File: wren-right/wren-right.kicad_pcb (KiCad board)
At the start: 2 copper layers, 93 parts, among them J1 TRRS_Jack, SW0 Reset, U1 ProMicro

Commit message: Tracks Finished
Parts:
- MX41: footprint MX_Only:MX-2U -> MX_Only:MX-2U-FLIPPED-ReversedStabilizers
- SW0: footprint random-keyboard-parts:SKQG-1155865 -> Button_Switch_THT:SW_PUSH_6mm; moved to F.Cu
- U1: moved to B.Cu
- moved R1 36.4 mm to (241.0, 33.8)
- moved R2 24.5 mm to (241.2, 46.0)
- moved SW0 3.97 mm to (238.1, 60.3)
- moved D13 2.38 mm to (190.5, 50.0)
- moved D3 2.38 mm to (190.5, 31.0)
- moved D23 2.38 mm to (190.5, 69.1)
- moved D33 2.38 mm to (190.5, 88.1)
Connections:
- U1 pad 1: COL8 -> ROW0
- U1 pad 10: ROW3 -> COL9
- U1 pad 11: ROW4 -> Net-(U1-Pad11)
- U1 pad 12: Net-(U1-Pad12) -> ROW4
- U1 pad 13: COL7 -> COL0
- U1 pad 14: COL6 -> COL1
- U1 pad 15: COL5 -> COL2
- U1 pad 16: COL4 -> COL3
- U1 pad 17: COL3 -> COL4
- U1 pad 18: COL2 -> COL5
- U1 pad 19: COL1 -> COL6
- U1 pad 2: COL9 -> ROW1
- U1 pad 20: COL0 -> COL7
- U1 pad 7: ROW0 -> ROW2
- U1 pad 8: ROW1 -> ROW3
- U1 pad 9: ROW2 -> COL8
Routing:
- net COL9: track 0.00 -> 265.9 mm, vias 0 -> 1
- net COL8: track 0.00 -> 247.9 mm, vias 0 -> 1
- net ROW3: track 0.00 -> 244.9 mm, vias 0 -> 1
- net ROW2: track 0.00 -> 227.9 mm, vias 0 -> 1
- net ROW1: track 0.00 -> 222.3 mm, vias 0 -> 1
- net ROW0: track 0.00 -> 211.7 mm, vias 0 -> 1
- net COL7: track 0.00 -> 210.2 mm, vias 0 -> 2
- net COL6: track 0.00 -> 192.4 mm, vias 0 -> 1
- net COL5: track 0.00 -> 170.9 mm, vias 0 -> 1
- net COL3: track 0.00 -> 164.6 mm
- net COL4: track 0.00 -> 152.9 mm, vias 0 -> 3
- net COL2: track 0.00 -> 149.9 mm, vias 0 -> 3
- net ROW4: track 0.00 -> 131.7 mm, vias 0 -> 1
- net COL1: track 0.00 -> 125.5 mm, vias 0 -> 1
- net COL0: track 0.00 -> 109.9 mm, vias 0 -> 1
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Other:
- board outline added: 230.3 x 117 mm

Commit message: Left Side Finished
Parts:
- removed D10, D17, D18, D19, D20, D27, D28, D29, D30, D37, D38, D39, D40, D7, D8, D9: D_Small, Diode_SMD:D_SOD-123
- removed MX10, MX17, MX18, MX19, MX20, MX27, MX28, MX29, MX30, MX37, MX38, MX39, MX40, MX7, MX8, MX9: MX-NoLED, MX_Only:MX-1U
- D1, D11, D12, D13, D14, D15, D16, D2, D21, D22, D23, D24, D25, D26, D3, D31, D32, D33, D34, D35, D36, D4, D41, D42, D43, D44, D5, D6, R1, R2, U1: moved to F.Cu
- J1, MX1, MX11, MX12, MX13, MX14, MX15, MX16, MX2, MX21, MX22, MX23, MX24, MX25, MX26, MX3, MX31, MX32, MX33, MX34, MX35, MX36, MX4, MX41, MX42, MX43, MX44, MX5, MX6, SW0: moved to B.Cu
- moved J1 198.3 mm to (58.4, 118.2), turned to 210 degrees
- moved D41 177.8 mm to (68.7, 130.1), turned to 30 degrees
- moved MX41 169.9 mm to (72.6, 137.3), turned to 120 degrees
- moved U1 169.9 mm to (72.6, 62.7)
- moved R2 169.7 mm to (72.8, 66.6), turned to 0 degrees
- moved R1 169.4 mm to (72.9, 54.4), turned to 0 degrees
- moved SW0 163.6 mm to (75.8, 80.9), turned to 180 degrees
- moved D1 144.7 mm to (85.3, 56.3)
- moved D11 144.7 mm to (85.3, 75.4)
- moved D21 144.7 mm to (85.3, 94.4)
- moved D31 144.7 mm to (85.3, 113.5)
- moved MX1 129.0 mm to (93.3, 56.3), turned to 180 degrees
- moved MX11 129.0 mm to (93.3, 75.4), turned to 180 degrees
- moved MX21 129.0 mm to (93.3, 94.4), turned to 180 degrees
- moved MX31 129.0 mm to (93.3, 113.5), turned to 180 degrees
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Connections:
- U1 pad 10: COL9 -> Net-(U1-Pad10)
- U1 pad 12: ROW4 -> Net-(U1-Pad12)
- U1 pad 19: COL6 -> Net-(U1-Pad19)
- U1 pad 20: COL7 -> Net-(U1-Pad20)
- U1 pad 9: COL8 -> Net-(U1-Pad9)
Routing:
- net COL9: track 265.9 -> 0.00 mm, vias 1 -> 0
- net COL8: track 247.9 -> 0.00 mm, vias 1 -> 0
- net ROW3: track 244.9 -> 0.00 mm, vias 1 -> 0
- net ROW2: track 227.9 -> 0.00 mm, vias 1 -> 0
- net ROW1: track 222.3 -> 0.00 mm, vias 1 -> 0
- net ROW0: track 211.7 -> 0.00 mm, vias 1 -> 0
- net COL7: track 210.2 -> 0.00 mm, vias 2 -> 0
- net COL6: track 192.4 -> 0.00 mm, vias 1 -> 0
- net COL5: track 170.9 -> 0.00 mm, vias 1 -> 0
- net COL3: track 164.6 -> 0.00 mm
- net COL4: track 152.9 -> 0.00 mm, vias 3 -> 0
- net COL2: track 149.9 -> 0.00 mm, vias 3 -> 0
- net ROW4: track 131.7 -> 0.00 mm, vias 1 -> 0
- net COL1: track 125.5 -> 0.00 mm, vias 1 -> 0
- net COL0: track 109.9 -> 0.00 mm, vias 1 -> 0
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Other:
- board size 230.3 x 117 mm -> 132.7 x 117 mm

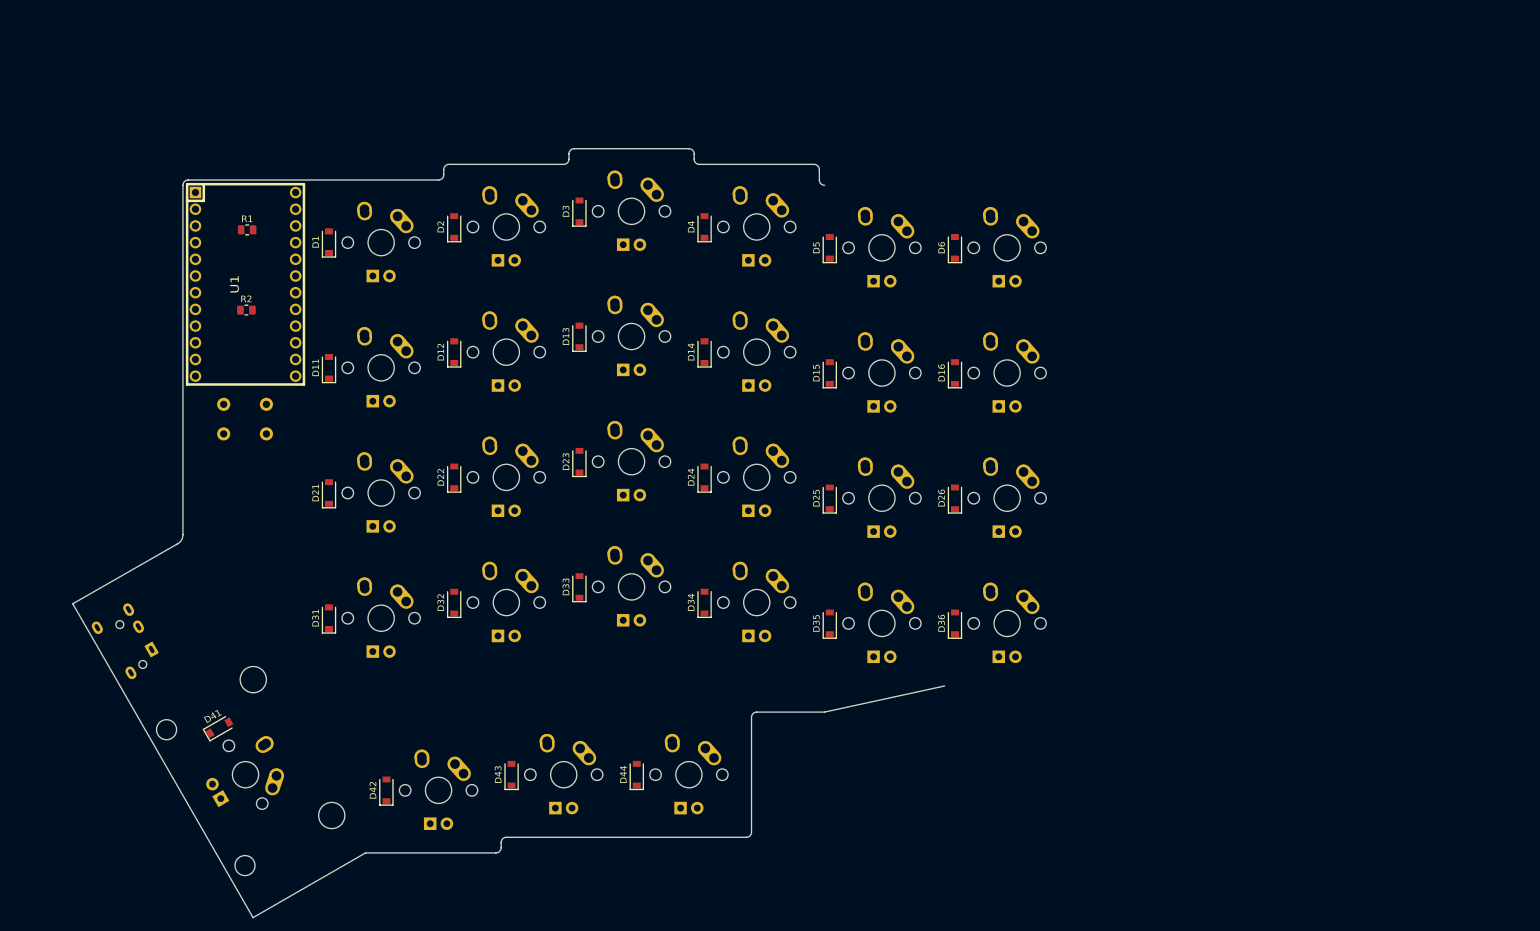
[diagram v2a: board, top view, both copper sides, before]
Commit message: Added Mirrored Right PCB
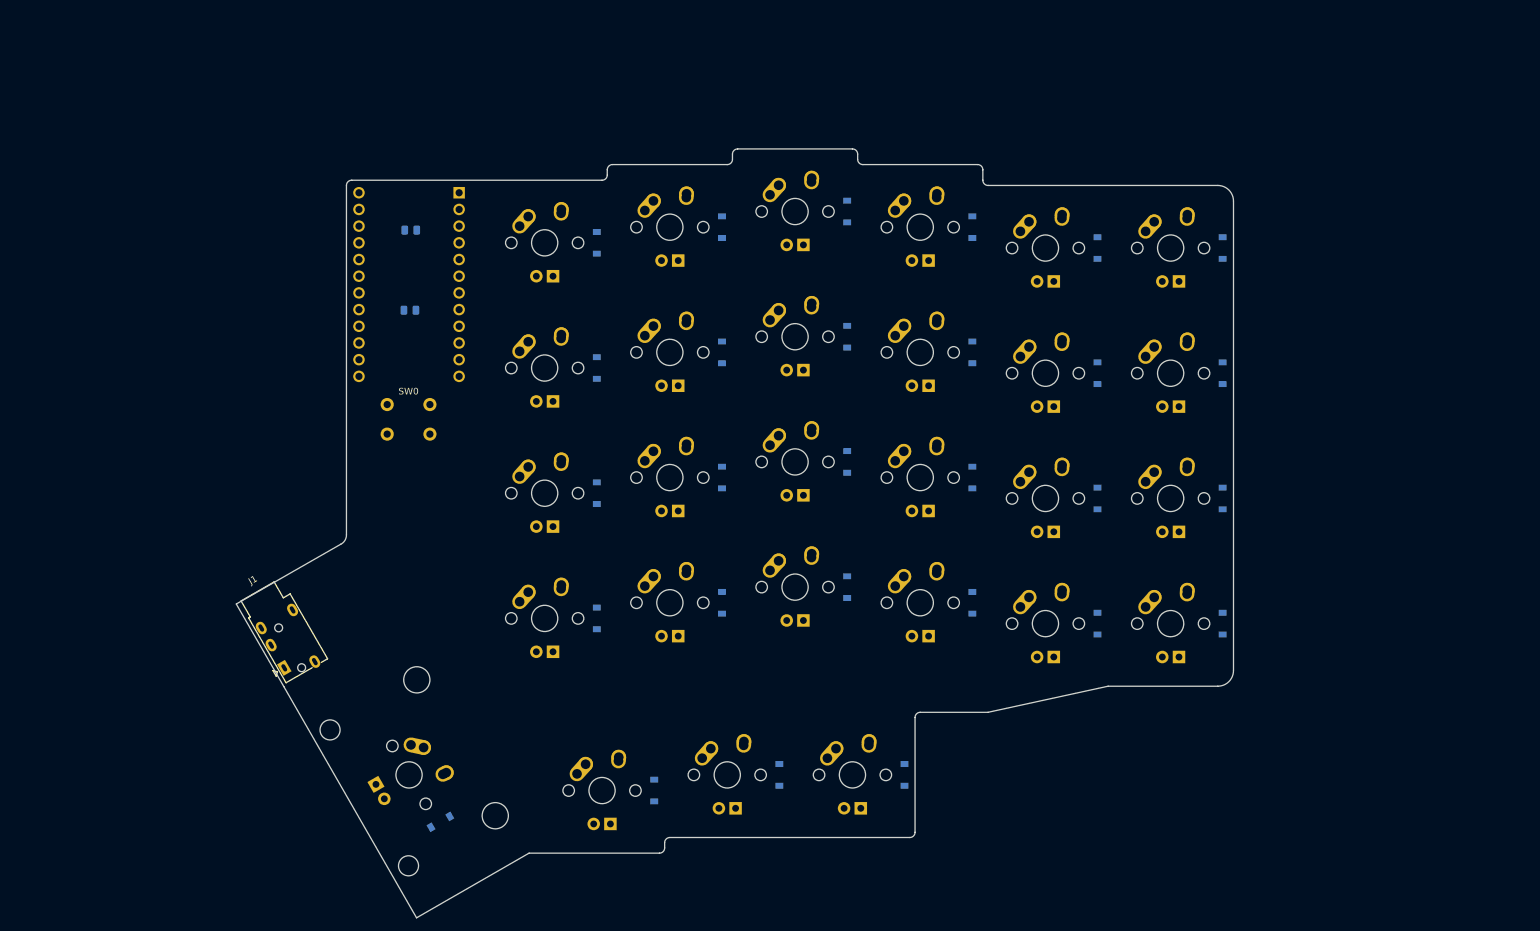
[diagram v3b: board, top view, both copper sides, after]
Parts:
- D1, D11, D12, D13, D14, D15, D16, D2, D21, D22, D23, D24, D25, D26, D3, D31, D32, D33, D34, D35, D36, D4, D41, D42, D43, D44, D5, D6, R1, R2, U1: moved to B.Cu
- J1, MX1, MX11, MX12, MX13, MX14, MX15, MX16, MX2, MX21, MX22, MX23, MX24, MX25, MX26, MX3, MX31, MX32, MX33, MX34, MX35, MX36, MX4, MX41, MX42, MX43, MX44, MX5, MX6: moved to F.Cu
- moved D1 40.8 mm to (126.1, 56.4)
- moved D11 40.8 mm to (126.1, 75.4)
- moved D21 40.8 mm to (126.1, 94.5)
- moved D31 40.8 mm to (126.1, 113.5)
- moved D42 40.8 mm to (134.8, 139.7)
- moved D12 40.8 mm to (145.1, 73.0)
- moved D2 40.8 mm to (145.1, 54.0)
- moved D22 40.8 mm to (145.1, 92.1)
- moved D32 40.8 mm to (145.1, 111.1)
- moved D43 40.7 mm to (153.9, 137.3)
- moved D13 40.7 mm to (164.2, 70.6)
- moved D23 40.7 mm to (164.2, 89.7)
- moved D3 40.7 mm to (164.2, 51.6)
- moved D33 40.7 mm to (164.2, 108.7)
- moved D44 40.7 mm to (172.9, 137.3)
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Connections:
- U1 pad 1: ROW0 -> (no net)
- U1 pad 10: Net-(U1-Pad10) -> ROW2
- U1 pad 11: Net-(U1-Pad11) -> ROW3
- U1 pad 12: Net-(U1-Pad12) -> ROW4
- U1 pad 19: Net-(U1-Pad19) -> (no net)
- U1 pad 2: ROW1 -> (no net)
- U1 pad 20: Net-(U1-Pad20) -> (no net)
- U1 pad 24: Net-(U1-Pad24) -> (no net)
- U1 pad 3: Net-(U1-Pad3) -> (no net)
- U1 pad 4: Net-(U1-Pad4) -> (no net)
- U1 pad 7: ROW2 -> (no net)
- U1 pad 8: ROW3 -> ROW0
- U1 pad 9: Net-(U1-Pad9) -> ROW1
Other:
- board size 132.7 x 117 mm -> 151.7 x 117 mm

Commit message: Wrap up for the day
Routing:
- net ROW1: track 0.00 -> 105.1 mm
- net ROW2: track 0.00 -> 103.7 mm
- net ROW0: track 0.00 -> 103.3 mm
- net ROW3: track 0.00 -> 103.3 mm
- net COL0: track 0.00 -> 89.1 mm
- net COL2: track 0.00 -> 87.2 mm
- net COL1: track 0.00 -> 85.2 mm
- net COL3: track 0.00 -> 82.9 mm
- net ROW4: track 0.00 -> 75.7 mm
- net COL5: track 0.00 -> 54.4 mm
- net COL4: track 0.00 -> 54.4 mm
- net Net-(D41-Pad2): track 0.00 -> 6.84 mm
- net Net-(D31-Pad2): track 0.00 -> 6.62 mm
- net Net-(D21-Pad2): track 0.00 -> 6.62 mm
- net Net-(D11-Pad2): track 0.00 -> 6.62 mm
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
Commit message: Add encoder to right side of schematic
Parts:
- moved R2 2.20 mm to (99.1, 68.3), turned to 270 degrees
- turned R1 to 180 degrees
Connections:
- U1 pad 1: (no net) -> Net-(U1-Pad1)
- U1 pad 10: ROW2 -> COL3
- U1 pad 11: ROW3 -> COL4
- U1 pad 12: ROW4 -> COL5
- U1 pad 13: COL0 -> ROW4
- U1 pad 14: COL1 -> ROW3
- U1 pad 15: COL2 -> ROW2
- U1 pad 16: COL3 -> ROW1
- U1 pad 17: COL4 -> ROW0
- U1 pad 18: COL5 -> Net-(U1-Pad18)
- U1 pad 19: (no net) -> Net-(U1-Pad19)
- U1 pad 2: (no net) -> Net-(U1-Pad2)
- U1 pad 20: (no net) -> Net-(U1-Pad20)
- U1 pad 24: (no net) -> Net-(U1-Pad24)
- U1 pad 3: (no net) -> Net-(U1-Pad3)
- U1 pad 4: (no net) -> Net-(U1-Pad4)
- U1 pad 7: (no net) -> COL0
- U1 pad 8: ROW0 -> COL1
- U1 pad 9: ROW1 -> COL2
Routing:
- net COL5: track 54.4 -> 164.2 mm, vias 0 -> 1
- net GND: track 0.00 -> 90.8 mm
- net COL4: track 54.4 -> 144.7 mm, vias 0 -> 1
- net VCC: track 0.00 -> 87.7 mm, vias 0 -> 2
- net SDA: track 0.00 -> 78.6 mm, vias 0 -> 1
- net SCL: track 0.00 -> 73.6 mm, vias 0 -> 3
- net ROW4: track 75.7 -> 148.8 mm
- net COL3: track 82.9 -> 154.6 mm, vias 0 -> 1
- net ROW3: track 103.3 -> 170.3 mm
- net COL2: track 87.2 -> 140.0 mm, vias 0 -> 1
- net ROW2: track 103.7 -> 155.4 mm
- net ROW1: track 105.1 -> 151.1 mm
- net ROW0: track 103.3 -> 143.8 mm
- net Net-(SW0-Pad1): track 0.00 -> 35.4 mm
- net COL1: track 85.2 -> 116.7 mm, vias 0 -> 1
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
